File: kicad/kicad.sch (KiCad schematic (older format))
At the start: 48 parts, among them J1 Power, J2 Address In, J3 Counter Reset Value, J4 5V, J5 Mode In, J6 GND, J7 VGA Out, J8 L77HDE15SD1CH4F, J9 Data In, U1 74LS157, U10 SN74LS682N, U11 74LS161, U12 74LS157, U13 74LS157, U14 74LS161, U15 74LS157, U16 74LS157, U17 74LS161, U18 SN74HC32N, U19 74LS161, U2 74LS157, U20 SN74LS04N, U21 AS6C4008-55PCN, U22 SN74LS74AN, U23 AS6C4008-55PCN, U24 SN74LS244N, U25 SN74LS244N, U26 SN74LS244N, U27 SN74LS244N, U28 SN74LS08N, U29 SN74LS04N, U3 SN74LS74AN, U4 SN74LS682N, U5 74LS157, U6 74LS157, U7 74LS161, U8 74LS157, U9 74LS157, X1 CXO_DIP8

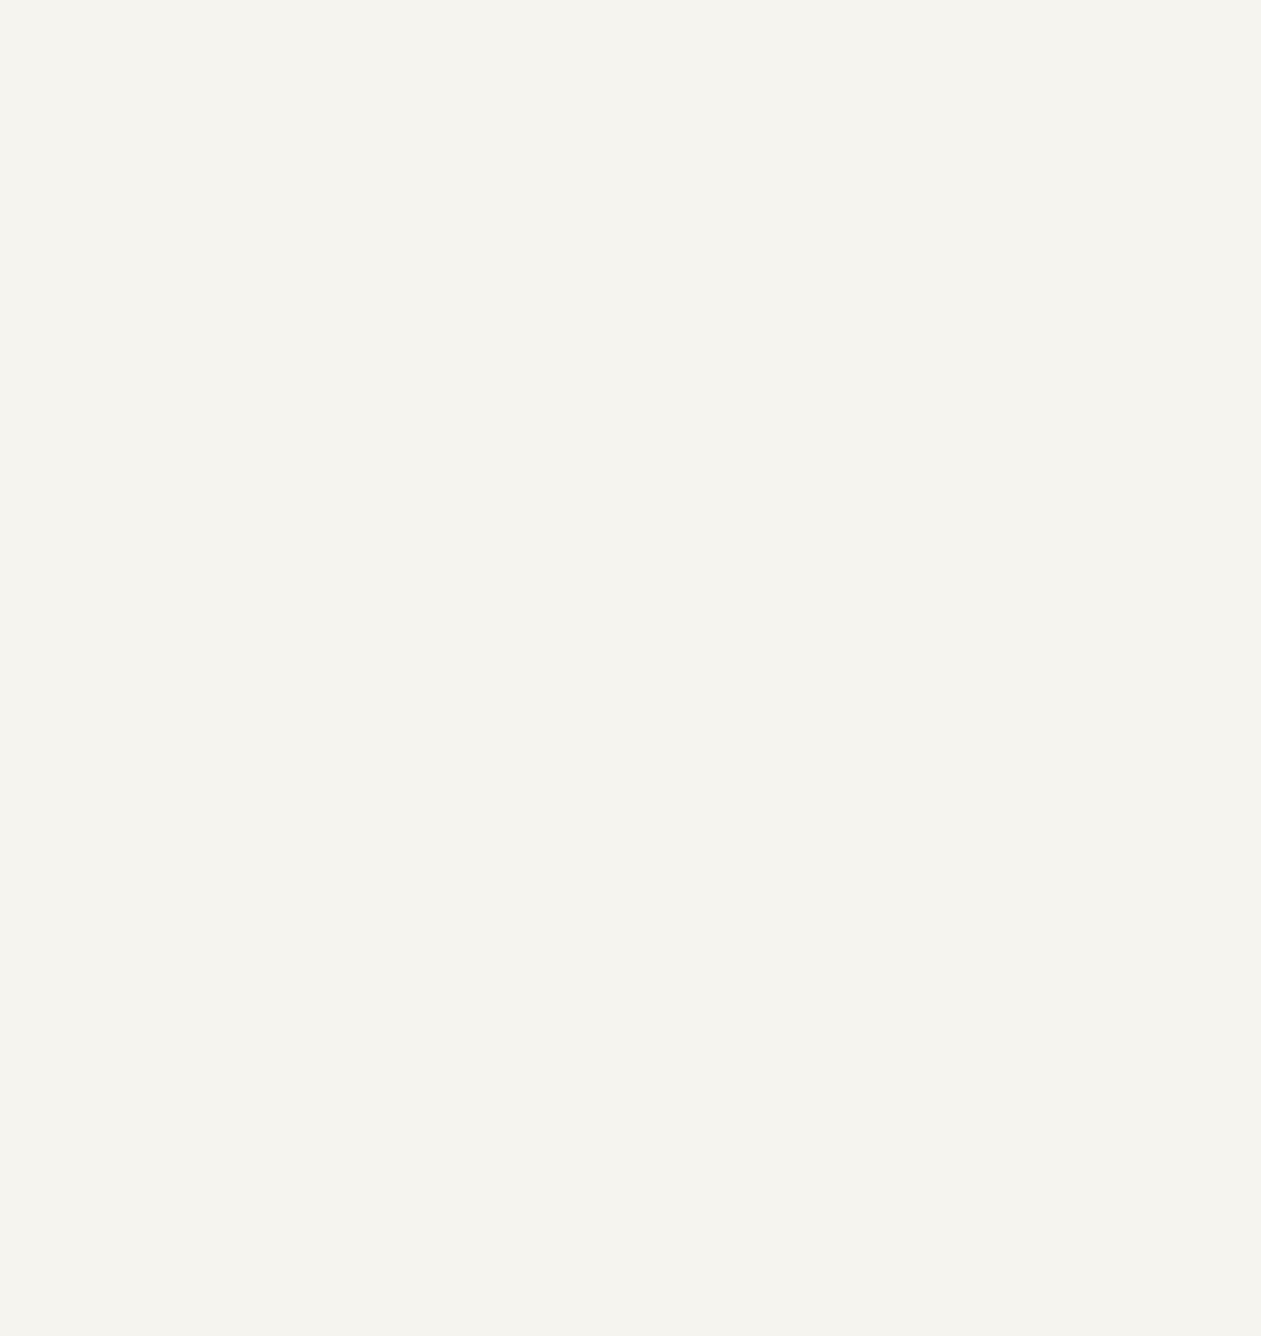
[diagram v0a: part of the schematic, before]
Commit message: Add caps and addl. power to schematic.
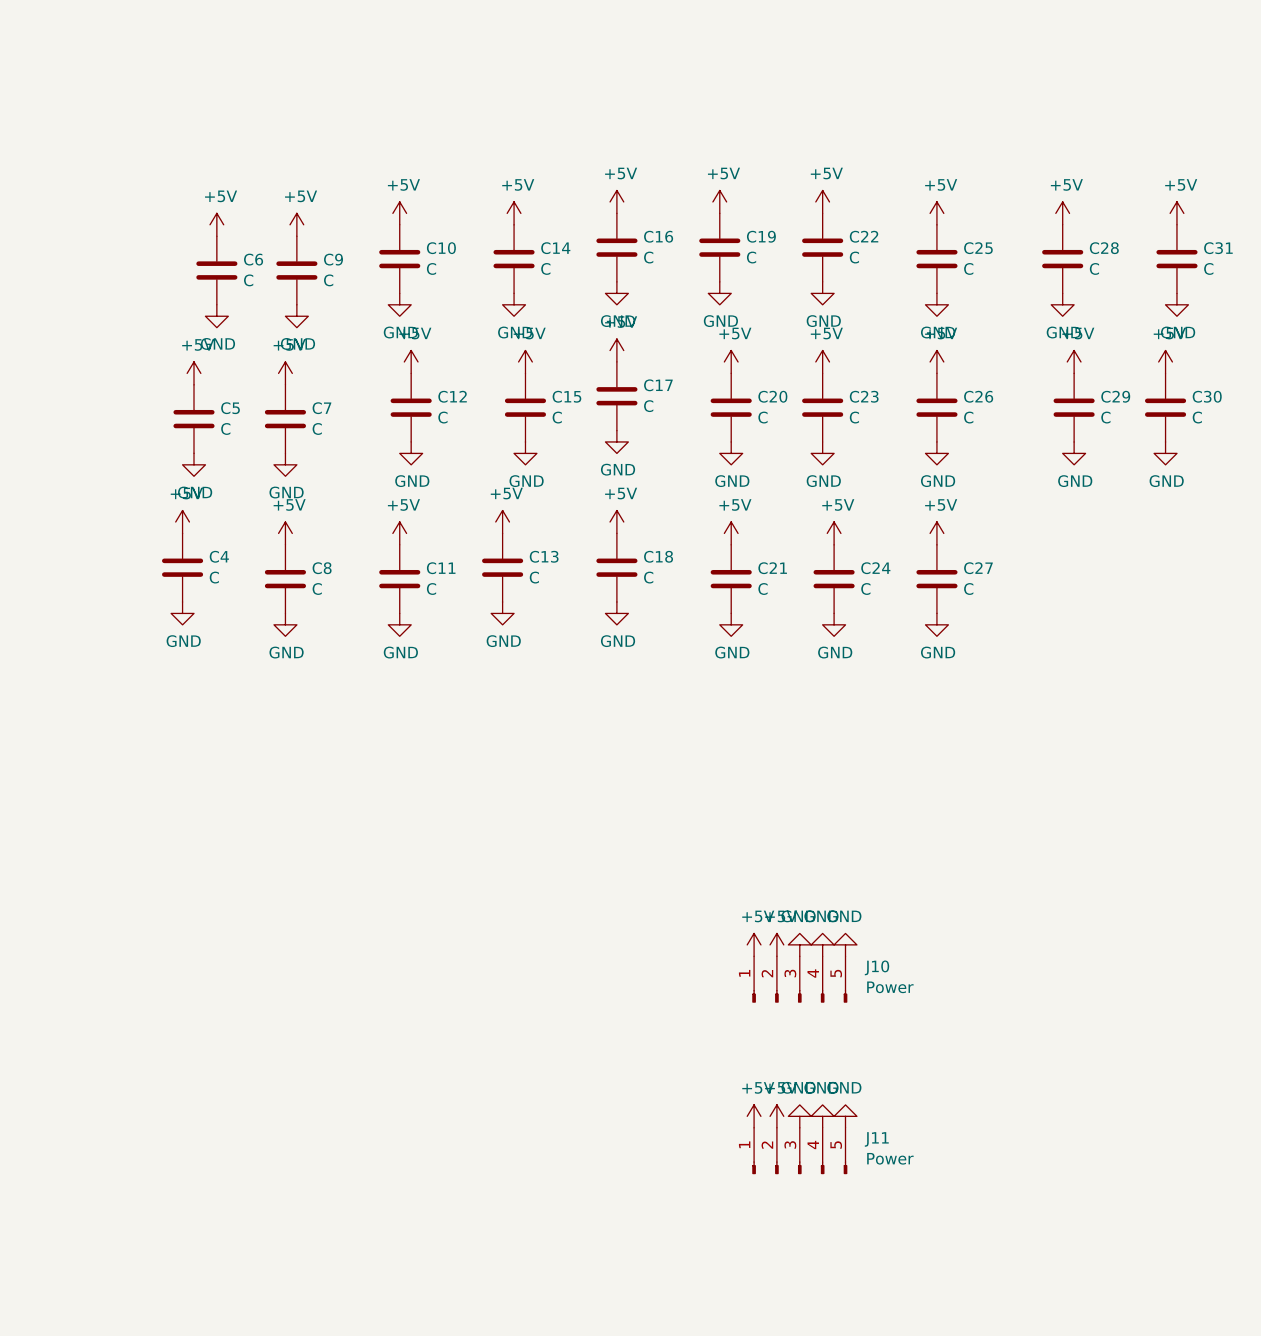
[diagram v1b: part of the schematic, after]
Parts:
- added C10, C11, C12, C13, C14, C15, C16, C17, C18, C19, C20, C21, C22, C23, C24, C25, C26, C27, C28, C29, C30, C31, C4, C5, C6, C7, C8, C9: C, Capacitor_THT:C_Disc_D3.0mm_W1.6mm_P2.50mm, symbol Device:C
- added J10, J11: Power, Connector_PinHeader_2.54mm:PinHeader_1x05_P2.54mm_Vertical, symbol Connector:Conn_01x05_Male
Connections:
- net +5V: now also C10.1, C11.1, C12.1, C13.1, C14.1, C15.1, C16.1, C17.1, C18.1, C19.1, C20.1, C21.1, C22.1, C23.1, C24.1, C25.1, C26.1, C27.1, C28.1, C29.1, C30.1, C31.1, C4.1, C5.1, C6.1, C7.1, C8.1, C9.1, J10.1 (Pin_1), J10.2 (Pin_2), J11.1 (Pin_1), J11.2 (Pin_2)
- net GND: now also C10.2, C11.2, C12.2, C13.2, C14.2, C15.2, C16.2, C17.2, C18.2, C19.2, C20.2, C21.2, C22.2, C23.2, C24.2, C25.2, C26.2, C27.2, C28.2, C29.2, C30.2, C31.2, C4.2, C5.2, C6.2, C7.2, C8.2, C9.2, J10.3 (Pin_3), J10.4 (Pin_4), J10.5 (Pin_5), J11.3 (Pin_3), J11.4 (Pin_4), J11.5 (Pin_5)
